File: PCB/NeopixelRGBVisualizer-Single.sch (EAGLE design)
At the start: 24 parts, among them CN2 5-12VDC, IC1 MSGEQ7, IC2 78L05ACZ-AP, Q1 16MHz, X1 STEREOJACK

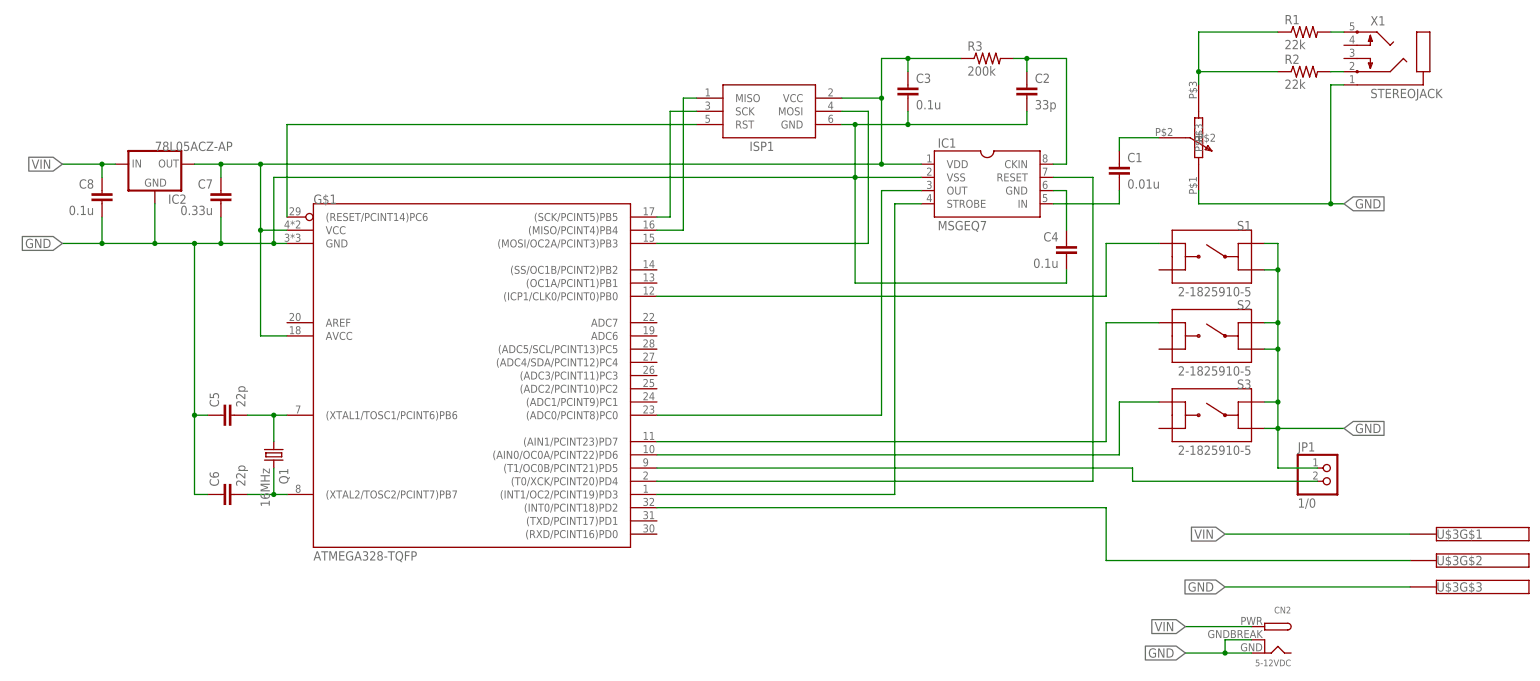
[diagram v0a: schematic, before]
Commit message: Found problem in proto2 board to be caused by knockoff MSGEQ7 chip. Maintained fixed pinouts of tactile switches and removed potentiometer from board.  Electrically, that circuit did not serve its purpose, and testing with multiple devices shows that the recommended configuration of the MSGEQ7 is fine for most consumer electronics.  Post-input gain processing will have to be managed with the tactile buttons. Added 1.5mm holes centered under each of the tactile buttons to locate pilot holes.
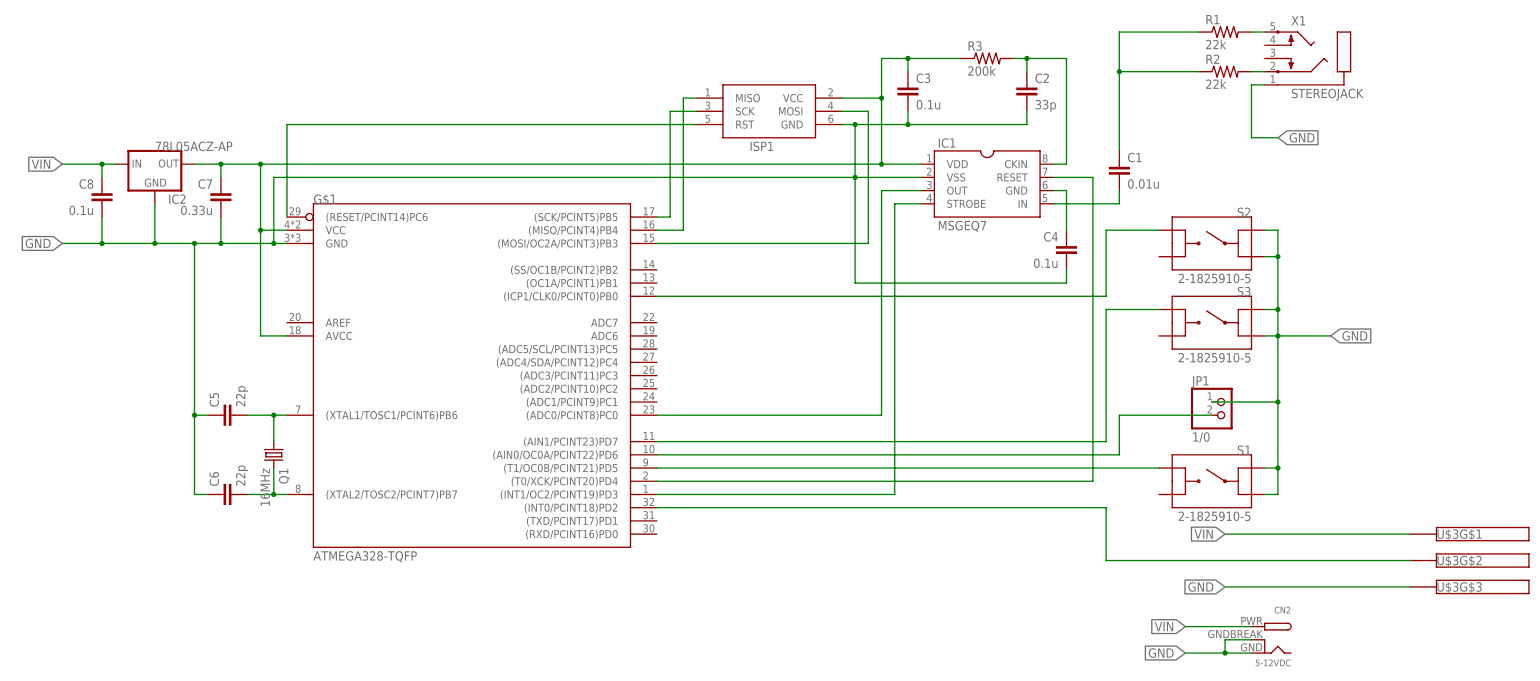
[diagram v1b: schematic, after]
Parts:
- removed U$2: PTD901-2015K, potentiometers:PTD901-2015K
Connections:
- removed net N$6: R1.1, R2.1, U$2.P$3
- net GND: no longer U$2.P$1
- net N$16: now also R1.1, R2.1; no longer U$2.P$2
- net N$18: now also S2.2; no longer S1.2
- net N$19: now also JP1.2; no longer S3.2
- net N$20: now also S1.2; no longer JP1.2
- net N$8: now also S3.2; no longer S2.2
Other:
- moved on the sheet: JP1, R1, R2, S1, S2, S3, X1
